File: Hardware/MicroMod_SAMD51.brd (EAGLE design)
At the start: 22 x 22 mm, 35 parts, among them J2 MICROMOD-2222, U1 W25QXX128MBIT-6X5-NO_CENTER, U2 ATSAMD51J20A-A, Y1 32.768kHz

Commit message: Adds gerbers of design
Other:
- board text added: "1"
- board text added: "2"
- board text added: "3"
- board text added: "4"
- board text added: "v10"
- board text removed: "v01"
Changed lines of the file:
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@@
 <setting verticaltext="up"/>
 </settings>
-<grid distance="1" unitdist="mm" unit="mm" style="lines" multiple="1" display="yes" altdistance="0.05" altunitdist="mm" altunit="mm"/>
+<grid distance="0.05" unitdist="inch" unit="inch" style="lines" multiple="1" display="yes" altdistance="0.005" altunitdist="inch" altunit="inch"/>
 <layers>
 <layer number="1" name="Top" color="4" fill="1" visible="yes" active="yes"/>
@@
 <layer number="19" name="Unrouted" color="6" fill="1" visible="yes" active="yes"/>
 <layer number="20" name="Dimension" color="15" fill="1" visible="yes" active="yes"/>
-<layer number="21" name="tPlace" color="16" fill="1" visible="no" active="yes"/>
-<layer number="22" name="bPlace" color="14" fill="1" visible="no" active="yes"/>
+<layer number="21" name="tPlace" color="16" fill="1" visible="yes" active="yes"/>
+<layer number="22" name="bPlace" color="14" fill="1" visible="yes" active="yes"/>
 <layer number="23" name="tOrigins" color="15" fill="1" visible="yes" active="yes"/>
 <layer number="24" name="bOrigins" color="15" fill="1" visible="yes" active="yes"/>
@@
 <layer number="38" name="bTest" color="7" fill="1" visible="no" active="yes"/>
 <layer number="39" name="tKeepout" color="4" fill="11" visible="no" active="yes"/>
-<layer number="40" name="bKeepout" color="1" fill="11" visible="yes" active="yes"/>
+<layer number="40" name="bKeepout" color="1" fill="11" visible="no" active="yes"/>
 <layer number="41" name="tRestrict" color="4" fill="10" visible="no" active="yes"/>
 <layer number="42" name="bRestrict" color="1" fill="10" visible="no" active="yes"/>
@@
 <wire x1="21.4" y1="4" x2="22" y2="4.6" width="0.05" layer="20" curve="86.784874"/>
 <wire x1="0" y1="4.6" x2="0.6" y2="4" width="0.05" layer="20" curve="86.784874"/>
-<text x="21.336" y="19.812" size="0.8128" layer="16" font="vector" ratio="20" rot="SMR270">v01</text>
+<text x="21.336" y="19.812" size="0.8128" layer="16" font="vector" ratio="20" rot="SMR270">v10</text>
 <text x="23.114" y="-14.097" size="1.778" layer="51" font="vector">Elias Santistevan</text>
 <wire x1="1" y1="22" x2="13.3" y2="22" width="0.05" layer="20"/>
@@
 <wire x1="13.3" y1="22" x2="15.05" y2="20.25" width="0.05" layer="20" curve="90"/>
 <wire x1="15.05" y1="20.25" x2="16.8" y2="22" width="0.05" layer="20" curve="90"/>
+<text x="5.461" y="20.701" size="0.762" layer="1" font="vector" ratio="15">1</text>
+<text x="5.461" y="20.701" size="0.762" layer="2" font="vector" ratio="15">2</text>
+<text x="5.461" y="20.701" size="0.762" layer="15" font="vector" ratio="15">3</text>
+<text x="5.842" y="20.701" size="0.762" layer="16" font="vector" ratio="15" rot="MR0">4</text>
 </plain>
 <attributes>

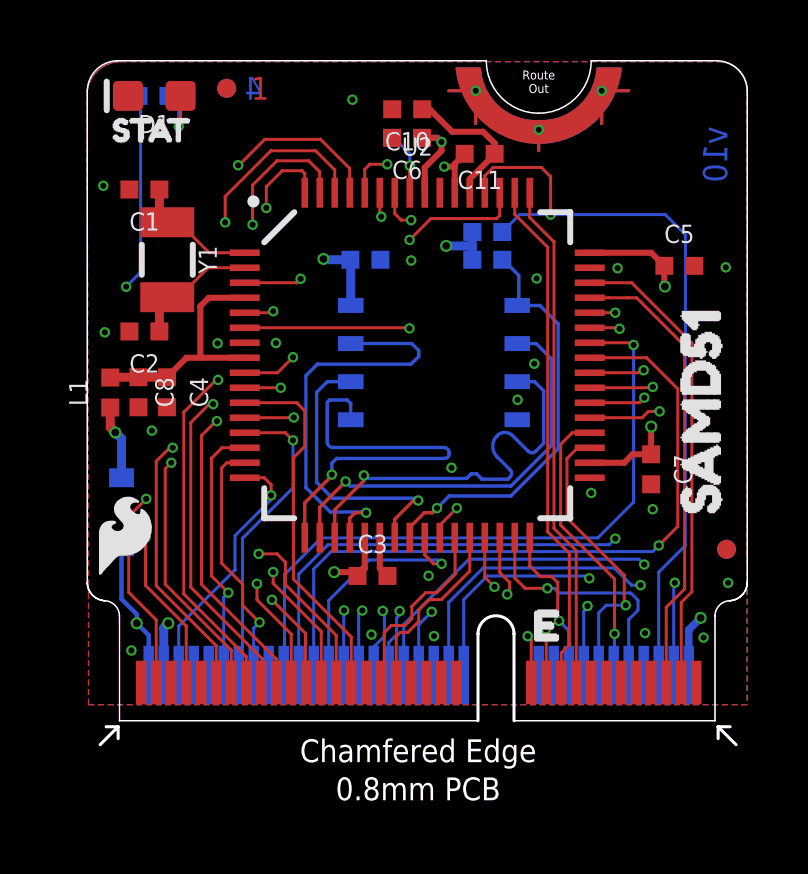
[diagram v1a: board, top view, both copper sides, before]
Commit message: Adds MicroMod logos
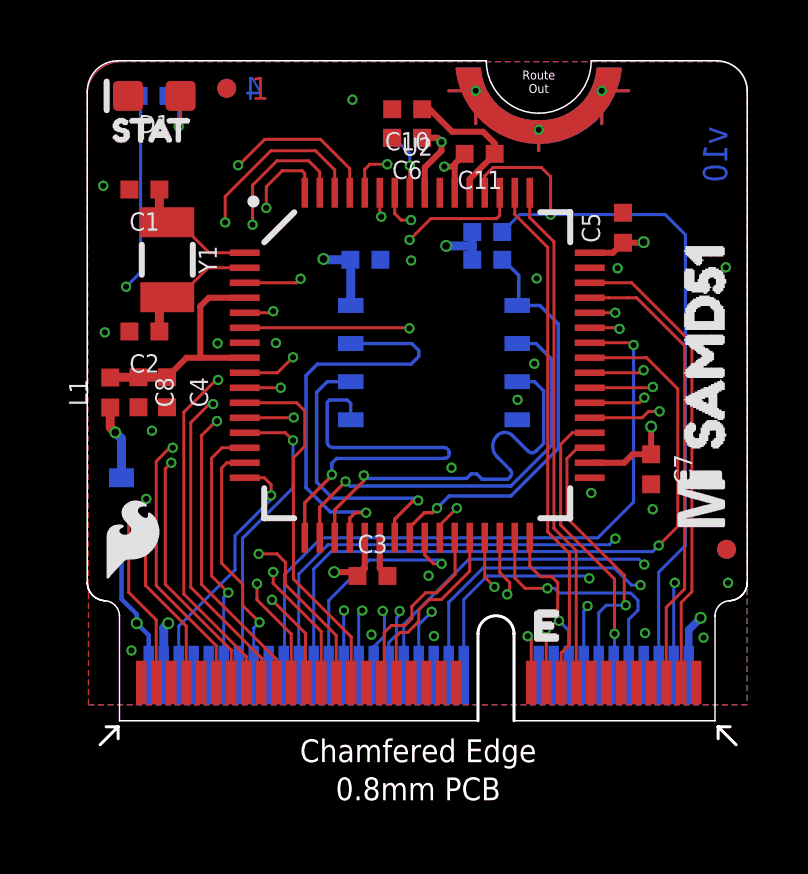
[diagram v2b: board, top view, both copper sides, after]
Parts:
- added U$1: (no value), SparkFun-MicroMod:MICROMOD_MI_LOGO_.35
- U$4: device Board Label:MICROMOD1 -> SparkFun-MicroMod:MICROMOD_LOGO_.35
- moved U$4 5.37 mm to (15.4, 4.95)
- moved C5 2.27 mm to (17.9, 16.4), turned to 90 degrees
- moved U$6 2.16 mm to (20.6, 7.87)
- moved U$7 0.28 mm to (1.50, 6.07)
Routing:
- net 3.3V: track 20.5 -> 19.1 mm
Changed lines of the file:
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@@
 <attribute name="VALUE" value="10uF" x="1.896" y="10.95" size="0.6096" layer="27" font="vector" ratio="20" rot="R270" align="top-center"/>
 </element>
-<element name="C5" library="SparkFun-Capacitors" package="0402-TIGHT" value="0.1uF" x="19.7358" y="15.1638" smashed="yes">
-<attribute name="NAME" x="19.7358" y="15.9258" size="0.6096" layer="25" font="vector" ratio="20" align="bottom-center"/>
-<attribute name="PROD_ID" value="CAP-15083" x="19.7358" y="15.1638" size="1.778" layer="27" font="vector" ratio="15" display="off"/>
-<attribute name="VALUE" x="19.7358" y="14.4018" size="0.6096" layer="27" font="vector" ratio="20" align="top-center"/>
+<element name="C5" library="SparkFun-Capacitors" package="0402-TIGHT" value="0.1uF" x="17.8562" y="16.4338" smashed="yes" rot="R90">
+<attribute name="NAME" x="17.0942" y="16.4338" size="0.6096" layer="25" font="vector" ratio="20" rot="R90" align="bottom-center"/>
+<attribute name="PROD_ID" value="CAP-15083" x="17.8562" y="16.4338" size="1.778" layer="27" font="vector" ratio="15" rot="R90" display="off"/>
+<attribute name="VALUE" x="18.6182" y="16.4338" size="0.6096" layer="27" font="vector" ratio="20" rot="R90" align="top-center"/>
 </element>
 <element name="C6" library="SparkFun-Capacitors" package="0402-TIGHT" value="0.1uF" x="10.664" y="19.4302" smashed="yes" rot="R180">
@@
 <attribute name="VALUE" x="13.081" y="19.4588" size="0.6096" layer="27" font="vector" ratio="20" rot="R180" align="top-center"/>
 </element>
-<element name="U$4" library="Board Label" package="MICROMOD1" value="" x="20.737" y="4.862" smashed="yes" rot="MR0"/>
 <element name="U$5" library="Board Label" package="SAMD510" value="" x="10.725" y="4.857" smashed="yes" rot="MR0"/>
-<element name="U$6" library="Board Label" package="SAMD510" value="" x="20.447" y="5.715" smashed="yes" rot="R90"/>
-<element name="U$7" library="SparkFun-Aesthetics" package="SFE_LOGO_FLAME_.1" value="" x="1.251" y="6.192" smashed="yes"/>
+<element name="U$6" library="Board Label" package="SAMD510" value="" x="20.574" y="7.874" smashed="yes" rot="R90"/>
+<element name="U$7" library="SparkFun-Aesthetics" package="SFE_LOGO_FLAME_.1" value="" x="1.505" y="6.065" smashed="yes"/>
 <element name="U$8" library="stat" package="STAT0" value="" x="0.127" y="19.685" smashed="yes"/>
 <element name="U2" library="SparkFun-IC-Microcontroller" package="TQFP64" value="ATSAMD51J20A-A" x="11" y="11.85" smashed="yes" rot="R270">
@@
 <attribute name="VALUE" x="1.905" y="6.95" size="0.6096" layer="28" font="vector" ratio="20" rot="MR270" align="top-center"/>
 </element>
+<element name="U$1" library="SparkFun-MicroMod" package="MICROMOD_MI_LOGO_.35" value="" x="20.447" y="7.366" smashed="yes" rot="R90"/>
+<element name="U$4" library="SparkFun-MicroMod" package="MICROMOD_LOGO_.35" value="" x="15.367" y="4.953" smashed="yes" rot="MR0"/>
 </elements>
 <signals>
@@
 <via x="8.2296" y="4.953" extent="1-16" drill="0.254"/>
 <via x="0.935" y="9.6098" extent="1-16" drill="0.254"/>
-<via x="19.2548" y="14.474" extent="1-16" drill="0.254"/>
+<via x="18.546" y="15.9528" extent="1-16" drill="0.254"/>
 <wire x1="18.796" y1="8.882" x2="18.796" y2="9.8044" width="0.2032" layer="1"/>
 <via x="18.796" y="9.8044" extent="1-16" drill="0.254"/>
@@
 <via x="11.9634" y="15.8282" extent="1-16" drill="0.254"/>
 <wire x1="16.75" y1="8.6" x2="17.899" y2="8.6" width="0.2032" layer="1"/>
-<wire x1="16.75" y1="15.6" x2="16.7502" y2="15.5998" width="0.2032" layer="1"/>
 <wire x1="11.25" y1="17.6" x2="11.25" y2="18.44" width="0.2032" layer="1"/>
 <wire x1="11.25" y1="18.44" x2="11.807" y2="18.997" width="0.2032" layer="1"/>
@@
 <wire x1="8.771" y1="15.367" x2="7.8994" y2="15.367" width="0.3" layer="16"/>
 <wire x1="7.8994" y1="15.367" x2="7.874" y2="15.3924" width="0.3" layer="16"/>
-<wire x1="18.7998" y1="15.5998" x2="19.2358" y2="15.1638" width="0.2032" layer="1"/>
-<wire x1="16.7502" y1="15.5998" x2="18.7998" y2="15.5998" width="0.2032" layer="1"/>
-<wire x1="19.2548" y1="14.474" x2="19.2358" y2="14.493" width="0.2032" layer="1"/>
-<wire x1="19.2358" y1="14.493" x2="19.2358" y2="15.1638" width="0.2032" layer="1"/>
 <wire x1="9.25" y1="6.1" x2="9.25" y2="5.07" width="0.2032" layer="1"/>
 <wire x1="9.25" y1="5.07" x2="9.006" y2="4.826" width="0.2032" layer="1"/>
@@
 <wire x1="1.143" y1="8.1" x2="1.143" y2="9.4018" width="0.3" layer="16"/>
 <wire x1="1.143" y1="9.4018" x2="0.935" y2="9.6098" width="0.3" layer="16"/>
+<wire x1="18.546" y1="15.9528" x2="18.527" y2="15.9338" width="0.2032" layer="1"/>
+<wire x1="18.527" y1="15.9338" x2="17.8562" y2="15.9338" width="0.2032" layer="1"/>
+<wire x1="16.75" y1="15.6" x2="17.5224" y2="15.6" width="0.2032" layer="1"/>
+<wire x1="17.5224" y1="15.6" x2="17.8562" y2="15.9338" width="0.2032" layer="1"/>
 </signal>
 <signal name="GND">

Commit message: Fills pin definitions  in variants, fixes I2S and D13 which were swapped (I2S Bus was crossing IOSETs)
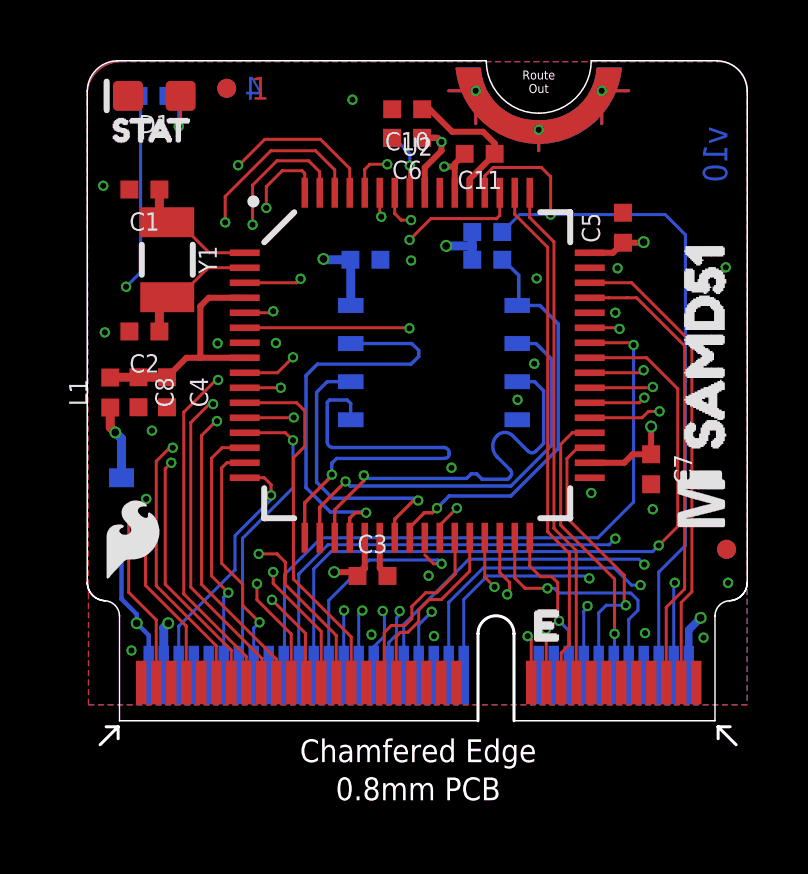
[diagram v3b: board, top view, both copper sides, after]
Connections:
- net D13: now also U2.25; no longer U2.44
- net I2S_CLK: now also U2.44; no longer U2.25
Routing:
- net D13: track 24.1 -> 23.3 mm
- net I2S_CLK: track 8.11 -> 7.54 mm
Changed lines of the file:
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@@
 <wire x1="1.2962" y1="14.4668" x2="1.778" y2="14.9486" width="0.1016" layer="16"/>
 <via x="1.2962" y="14.4668" extent="1-16" drill="0.2"/>
-<contactref element="U2" pad="44"/>
-<wire x1="16.75" y1="13.6" x2="17.6" y2="13.6" width="0.1016" layer="1"/>
 <via x="17.6" y="13.6" extent="1-16" drill="0.2"/>
 <wire x1="15.8048" y1="14.3952" x2="1.3678" y2="14.3952" width="0.1016" layer="2"/>
@@
 <wire x1="17.6" y1="13.6" x2="16.6" y2="13.6" width="0.1016" layer="2"/>
 <wire x1="16.6" y1="13.6" x2="15.8048" y2="14.3952" width="0.1016" layer="2"/>
+<contactref element="U2" pad="25"/>
+<wire x1="17.6" y1="13.6" x2="11.25" y2="6.1" width="0" layer="19" extent="1-1"/>
 </signal>
 <signal name="D2">
@@
 <wire x1="11.68463125" y1="5.3594" x2="9.398" y2="5.3594" width="0.1016" layer="16"/>
 <wire x1="9.398" y1="5.3594" x2="8.049" y2="4.0104" width="0.1016" layer="16"/>
-<contactref element="U2" pad="25"/>
 <wire x1="11.81163125" y1="5.2324" x2="11.5476" y2="5.2324" width="0.1016" layer="1"/>
-<wire x1="11.25" y1="5.53" x2="11.25" y2="6.1" width="0.1016" layer="1"/>
 <wire x1="11.5476" y1="5.2324" x2="11.25" y2="5.53" width="0.1016" layer="1"/>
+<contactref element="U2" pad="44"/>
+<wire x1="11.81163125" y1="5.2324" x2="16.75" y2="13.6" width="0" layer="19" extent="1-1"/>
 </signal>
 <signal name="D5">

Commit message: Changes so that SPI and I2C work
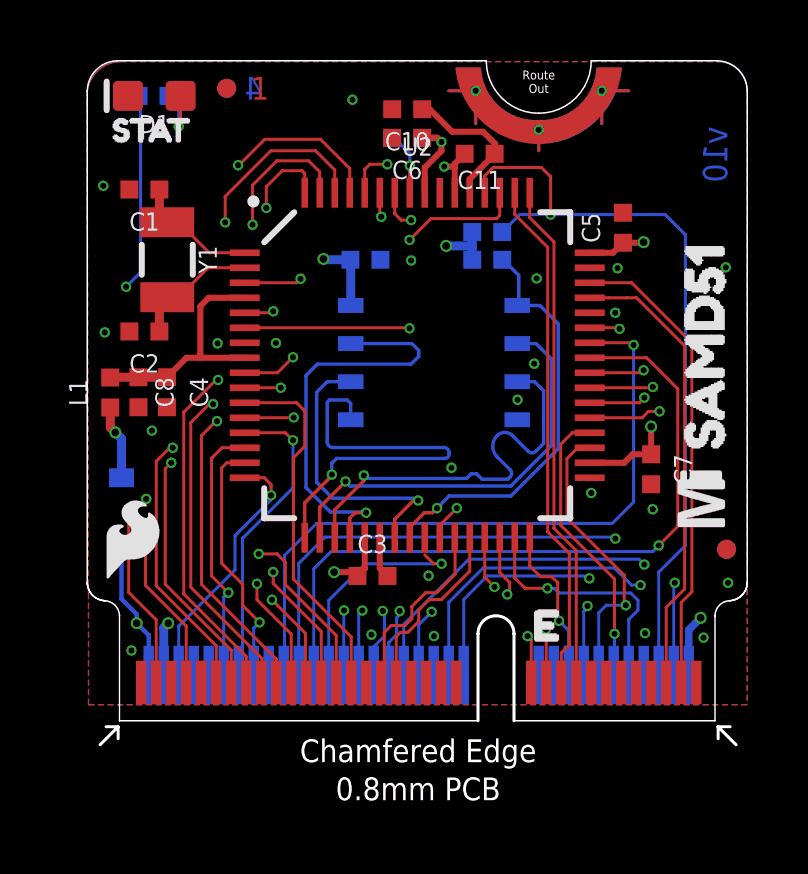
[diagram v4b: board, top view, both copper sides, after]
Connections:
- net D13: now also U2.44; no longer U2.25
- net I2S_CLK: now also U2.25; no longer U2.44
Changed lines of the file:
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@@
 <setting verticaltext="up"/>
 </settings>
-<grid distance="0.05" unitdist="inch" unit="inch" style="lines" multiple="1" display="yes" altdistance="0.005" altunitdist="inch" altunit="inch"/>
+<grid distance="0.01" unitdist="inch" unit="inch" style="lines" multiple="1" display="yes" altdistance="0.001" altunitdist="inch" altunit="inch"/>
 <layers>
 <layer number="1" name="Top" color="4" fill="1" visible="yes" active="yes"/>
-<layer number="2" name="PWR_HORIZ" color="1" fill="3" visible="yes" active="yes"/>
-<layer number="15" name="GND-VERT" color="4" fill="6" visible="yes" active="yes"/>
+<layer number="2" name="PWR_HORIZ" color="1" fill="3" visible="no" active="yes"/>
+<layer number="15" name="GND-VERT" color="4" fill="6" visible="no" active="yes"/>
 <layer number="16" name="Bottom" color="3" fill="1" visible="yes" active="yes"/>
 <layer number="17" name="Pads" color="26" fill="1" visible="yes" active="yes"/>
@@
 <layer number="19" name="Unrouted" color="6" fill="1" visible="yes" active="yes"/>
 <layer number="20" name="Dimension" color="15" fill="1" visible="yes" active="yes"/>
-<layer number="21" name="tPlace" color="16" fill="1" visible="yes" active="yes"/>
-<layer number="22" name="bPlace" color="14" fill="1" visible="yes" active="yes"/>
+<layer number="21" name="tPlace" color="16" fill="1" visible="no" active="yes"/>
+<layer number="22" name="bPlace" color="14" fill="1" visible="no" active="yes"/>
 <layer number="23" name="tOrigins" color="15" fill="1" visible="yes" active="yes"/>
 <layer number="24" name="bOrigins" color="15" fill="1" visible="yes" active="yes"/>
@@
 <layer number="37" name="tTest" color="7" fill="1" visible="no" active="yes"/>
 <layer number="38" name="bTest" color="7" fill="1" visible="no" active="yes"/>
-<layer number="39" name="tKeepout" color="4" fill="11" visible="no" active="yes"/>
+<layer number="39" name="tKeepout" color="4" fill="11" visible="yes" active="yes"/>
 <layer number="40" name="bKeepout" color="1" fill="11" visible="no" active="yes"/>
 <layer number="41" name="tRestrict" color="4" fill="10" visible="no" active="yes"/>
@@
 <wire x1="17.6" y1="13.6" x2="16.6" y2="13.6" width="0.1016" layer="2"/>
 <wire x1="16.6" y1="13.6" x2="15.8048" y2="14.3952" width="0.1016" layer="2"/>
-<contactref element="U2" pad="25"/>
-<wire x1="17.6" y1="13.6" x2="11.25" y2="6.1" width="0" layer="19" extent="1-1"/>
+<contactref element="U2" pad="44"/>
+<wire x1="17.6" y1="13.6" x2="16.75" y2="13.6" width="0" layer="19" extent="1-1"/>
 </signal>
 <signal name="D2">
@@
 <signal name="I2S_SDO">
 <contactref element="J2" pad="56"/>
-<wire x1="6.5744" y1="4.8726" x2="6.5744" y2="1.5504" width="0.1016" layer="16"/>
+<wire x1="6.5744" y1="5.5076" x2="6.5744" y2="1.5504" width="0.1016" layer="16"/>
 <wire x1="6.549" y1="1.525" x2="6.5744" y2="1.5504" width="0.1016" layer="16"/>
-<wire x1="17.018" y1="6.096" x2="18.2118" y2="7.2898" width="0.1016" layer="16"/>
+<wire x1="17.5006" y1="6.5786" x2="18.2118" y2="7.2898" width="0.1016" layer="16"/>
 <wire x1="18.2118" y1="7.2898" x2="18.2118" y2="12.5254" width="0.1016" layer="16"/>
 <via x="18.2118" y="12.5254" extent="1-16" drill="0.2"/>
-<wire x1="6.5744" y1="4.8726" x2="7.7978" y2="6.096" width="0.1016" layer="16"/>
-<wire x1="7.7978" y1="6.096" x2="17.018" y2="6.096" width="0.1016" layer="16"/>
+<wire x1="6.5744" y1="5.5076" x2="7.6454" y2="6.5786" width="0.1016" layer="16"/>
+<wire x1="7.6454" y1="6.5786" x2="17.5006" y2="6.5786" width="0.1016" layer="16"/>
 <contactref element="U2" pad="42"/>
 <wire x1="16.75" y1="12.6" x2="18.1372" y2="12.6" width="0.1016" layer="1"/>
@@
 <wire x1="17.743" y1="13.0626" x2="17.743" y2="6.2114" width="0.1016" layer="15"/>
 <via x="17.6022" y="6.0706" extent="1-16" drill="0.2"/>
-<wire x1="7.049" y1="1.525" x2="7.049" y2="4.89" width="0.1016" layer="16"/>
-<wire x1="7.049" y1="4.89" x2="8.0264" y2="5.8674" width="0.1016" layer="16"/>
-<wire x1="17.399" y1="5.8674" x2="17.6022" y2="6.0706" width="0.1016" layer="16"/>
-<wire x1="8.0264" y1="5.8674" x2="17.399" y2="5.8674" width="0.1016" layer="16"/>
+<wire x1="7.049" y1="1.525" x2="7.049" y2="5.2456" width="0.1016" layer="16"/>
+<wire x1="7.049" y1="5.2456" x2="7.9248" y2="6.1214" width="0.1016" layer="16"/>
+<wire x1="17.5514" y1="6.1214" x2="17.6022" y2="6.0706" width="0.1016" layer="16"/>
+<wire x1="17.5514" y1="6.1214" x2="7.9248" y2="6.1214" width="0.1016" layer="16"/>
 <contactref element="U2" pad="43"/>
 <wire x1="16.75" y1="13.1" x2="17.7056" y2="13.1" width="0.1016" layer="1"/>
@@
 <wire x1="8.049" y1="1.525" x2="8.049" y2="4.0104" width="0.1016" layer="16"/>
 <via x="11.81163125" y="5.2324" extent="1-16" drill="0.2"/>
-<wire x1="11.81163125" y1="5.2324" x2="11.68463125" y2="5.3594" width="0.1016" layer="16"/>
-<wire x1="11.68463125" y1="5.3594" x2="9.398" y2="5.3594" width="0.1016" layer="16"/>
-<wire x1="9.398" y1="5.3594" x2="8.049" y2="4.0104" width="0.1016" layer="16"/>
+<wire x1="11.81163125" y1="5.2324" x2="9.271" y2="5.2324" width="0.1016" layer="16"/>
+<wire x1="9.271" y1="5.2324" x2="8.049" y2="4.0104" width="0.1016" layer="16"/>
 <wire x1="11.81163125" y1="5.2324" x2="11.5476" y2="5.2324" width="0.1016" layer="1"/>
 <wire x1="11.5476" y1="5.2324" x2="11.25" y2="5.53" width="0.1016" layer="1"/>
-<contactref element="U2" pad="44"/>
-<wire x1="11.81163125" y1="5.2324" x2="16.75" y2="13.6" width="0" layer="19" extent="1-1"/>
+<contactref element="U2" pad="25"/>
+<wire x1="11.25" y1="5.53" x2="11.25" y2="6.1" width="0" layer="19" extent="1-1"/>
 </signal>
 <signal name="D5">
